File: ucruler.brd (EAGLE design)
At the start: 200 x 32 mm, 46 parts

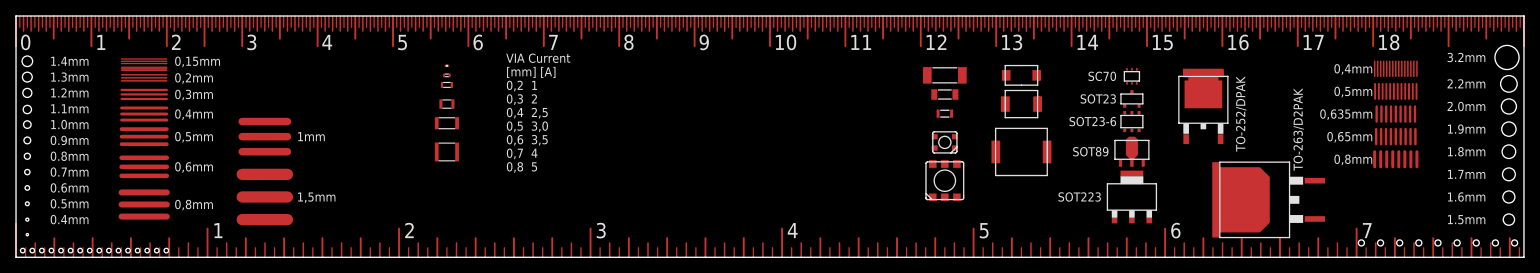
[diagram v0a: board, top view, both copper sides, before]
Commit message: labeled all packages
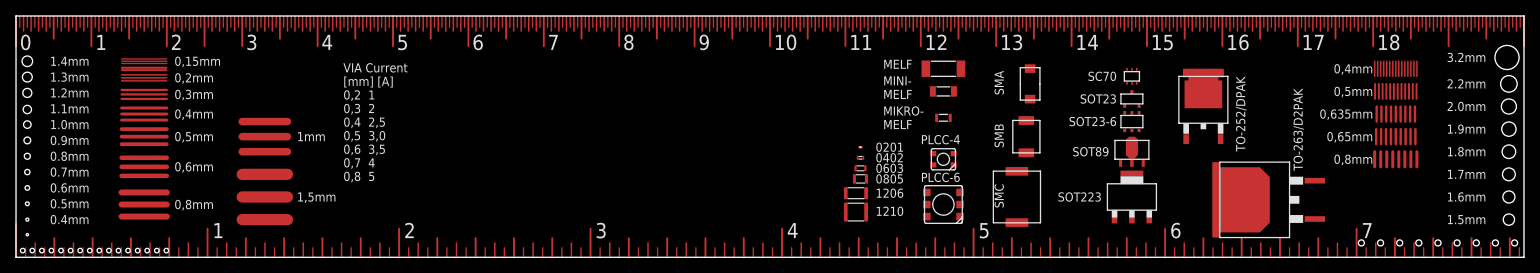
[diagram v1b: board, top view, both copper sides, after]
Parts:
- moved E$43 56.0 mm to (112.0, 11.8), turned to 180 degrees
- moved E$42 55.9 mm to (112.0, 13.2), turned to 180 degrees
- moved E$41 55.9 mm to (112.0, 14.6), turned to 180 degrees
- moved E$44 55.7 mm to (112.0, 10.4), turned to 180 degrees
- moved E$45 55.0 mm to (111.4, 8.50)
- moved E$46 54.8 mm to (111.4, 6.00)
- moved E$34 6.00 mm to (132.8, 8.00), turned to 180 degrees
- moved E$33 4.37 mm to (134.0, 16.0), turned to 180 degrees
- moved E$40 3.17 mm to (123.0, 7.00), turned to 90 degrees
- moved E$39 2.25 mm to (123.0, 13.0)
- moved E$35 1.61 mm to (134.5, 23.0), turned to 180 degrees
- moved E$36 0.89 mm to (123.0, 25.0)
- moved E$38 0.58 mm to (123.0, 18.5), turned to 270 degrees
- moved E$37 0.45 mm to (123.0, 22.0), turned to 270 degrees
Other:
- board text added: "0201"
- board text added: "0402"
- board text added: "0603"
- board text added: "0805"
- board text added: "1206"
- board text added: "1210"
- board text added: "MELF"
- board text added: "MIKRO- MELF"
- board text added: "MINI- MELF"
- board text added: "PLCC-4"
- board text added: "PLCC-6"
- board text added: "SMA"
- board text added: "SMB"
- board text added: "SMC"
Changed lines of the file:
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@@
 <setting verticaltext="up"/>
 </settings>
-<grid distance="0.05" unitdist="inch" unit="mm" style="lines" multiple="1" display="yes" altdistance="0.025" altunitdist="inch" altunit="mm"/>
+<grid distance="1" unitdist="mm" unit="mm" style="lines" multiple="1" display="yes" altdistance="0.25" altunitdist="mm" altunit="mm"/>
 <layers>
 <layer number="1" name="Top" color="4" fill="1" visible="yes" active="yes"/>
@@
 <layer number="14" name="Route14" color="1" fill="6" visible="no" active="no"/>
 <layer number="15" name="Route15" color="4" fill="6" visible="no" active="no"/>
-<layer number="16" name="Bottom" color="1" fill="1" visible="no" active="yes"/>
+<layer number="16" name="Bottom" color="1" fill="1" visible="yes" active="yes"/>
 <layer number="17" name="Pads" color="2" fill="1" visible="yes" active="yes"/>
 <layer number="18" name="Vias" color="2" fill="1" visible="yes" active="yes"/>
@@
 <hole x="193.675" y="1.905" drill="0.8"/>
 <hole x="191.135" y="1.905" drill="0.8"/>
-<text x="65" y="27" size="1.2" layer="21" align="top-left">VIA Current
+<text x="43.41" y="25.73" size="1.2" layer="21" align="top-left">VIA Current
 [mm] [A]
 0,2  1
@@
 <text x="162.43" y="14.02" size="1.2" layer="21" font="fixed" rot="R270" align="center-right">TO-252/DPAK</text>
 <text x="170.05" y="11.48" size="1.2" layer="21" font="fixed" rot="R270" align="center-right">TO-263/D2PAK</text>
+<text x="114" y="5.5" size="1.2" layer="21" ratio="10">1210</text>
+<text x="114" y="7.9" size="1.2" layer="21" ratio="10">1206</text>
+<text x="114" y="14" size="1.2" layer="21" ratio="10">0201</text>
+<text x="114" y="12.6" size="1.2" layer="21" ratio="10">0402</text>
+<text x="114" y="11.2" size="1.2" layer="21" ratio="10">0603</text>
+<text x="114" y="9.8" size="1.2" layer="21" ratio="10">0805</text>
+<text x="131" y="21.5" size="1.2" layer="21" ratio="10" rot="R90">SMA</text>
+<text x="131" y="14.5" size="1.2" layer="21" ratio="10" rot="R90">SMB</text>
+<text x="131" y="6.5" size="1.2" layer="21" ratio="10" rot="R90">SMC</text>
+<text x="115" y="25" size="1.2" layer="21" ratio="10">MELF</text>
+<text x="115" y="21" size="1.2" layer="21" ratio="10">MINI-
+MELF</text>
+<text x="115" y="17" size="1.2" layer="21" ratio="10">MIKRO-
+MELF</text>
+<text x="120" y="15" size="1.2" layer="21" ratio="10">PLCC-4</text>
+<text x="120" y="10" size="1.2" layer="21" ratio="10">PLCC-6</text>
 </plain>
 <attributes>
@@
 <element name="E$31" library="ucruler" package="PACK-TO252" value="" x="157.48" y="17.78"/>
 <element name="E$32" library="ucruler" package="PACK-TO263" value="" x="168.91" y="7.62" rot="R90"/>
-<element name="E$33" library="ucruler" package="PACK-DO214AA-SMB" value="" x="133.35" y="20.32" rot="R90"/>
-<element name="E$34" library="ucruler" package="PACK-DO214AB-SMC" value="" x="133.35" y="13.97" rot="R90"/>
-<element name="E$35" library="ucruler" package="PACK-DO214AC-SMA" value="" x="133.35" y="24.13" rot="R90"/>
-<element name="E$36" library="ucruler" package="PACK-MELF" value="" x="123.19" y="24.13" rot="R90"/>
-<element name="E$37" library="ucruler" package="PACK-MELF-MINI" value="" x="123.19" y="21.59" rot="R90"/>
-<element name="E$38" library="ucruler" package="PACK-MELF-MICRO" value="" x="123.19" y="19.05" rot="R90"/>
-<element name="E$39" library="ucruler" package="PACK-PLCC-4" value="" x="123.19" y="15.24" rot="R90"/>
-<element name="E$40" library="ucruler" package="PACK-PLCC-6" value="" x="123.19" y="10.16"/>
-<element name="E$41" library="ucruler" package="PACK-0201" value="" x="57.15" y="25.4"/>
-<element name="E$42" library="ucruler" package="PACK-0402" value="" x="57.15" y="24.13"/>
-<element name="E$43" library="ucruler" package="PACK-0603" value="" x="57.15" y="22.86"/>
-<element name="E$44" library="ucruler" package="PACK-0805" value="" x="57.15" y="20.32"/>
-<element name="E$45" library="ucruler" package="PACK-1206" value="" x="57.15" y="17.78"/>
-<element name="E$46" library="ucruler" package="PACK-1210" value="" x="57.15" y="13.97"/>
+<element name="E$33" library="ucruler" package="PACK-DO214AA-SMB" value="" x="134" y="16" rot="R180"/>
+<element name="E$34" library="ucruler" package="PACK-DO214AB-SMC" value="" x="132.75" y="8" rot="R180"/>
+<element name="E$35" library="ucruler" package="PACK-DO214AC-SMA" value="" x="134.5" y="23" rot="R180"/>
+<element name="E$36" library="ucruler" package="PACK-MELF" value="" x="123" y="25" rot="R90"/>
+<element name="E$37" library="ucruler" package="PACK-MELF-MINI" value="" x="123" y="22" rot="R270"/>
+<element name="E$38" library="ucruler" package="PACK-MELF-MICRO" value="" x="123" y="18.5" rot="R270"/>
+<element name="E$39" library="ucruler" package="PACK-PLCC-4" value="" x="123" y="13" rot="R90"/>
+<element name="E$40" library="ucruler" package="PACK-PLCC-6" value="" x="123" y="7" rot="R90"/>
+<element name="E$41" library="ucruler" package="PACK-0201" value="" x="112" y="14.6" rot="R180"/>
+<element name="E$42" library="ucruler" package="PACK-0402" value="" x="112" y="13.2" rot="R180"/>
+<element name="E$43" library="ucruler" package="PACK-0603" value="" x="112" y="11.8" rot="R180"/>
+<element name="E$44" library="ucruler" package="PACK-0805" value="" x="112" y="10.4" rot="R180"/>
+<element name="E$45" library="ucruler" package="PACK-1206" value="" x="111.4" y="8.5"/>
+<element name="E$46" library="ucruler" package="PACK-1210" value="" x="111.4" y="6"/>
 </elements>
 <signals>

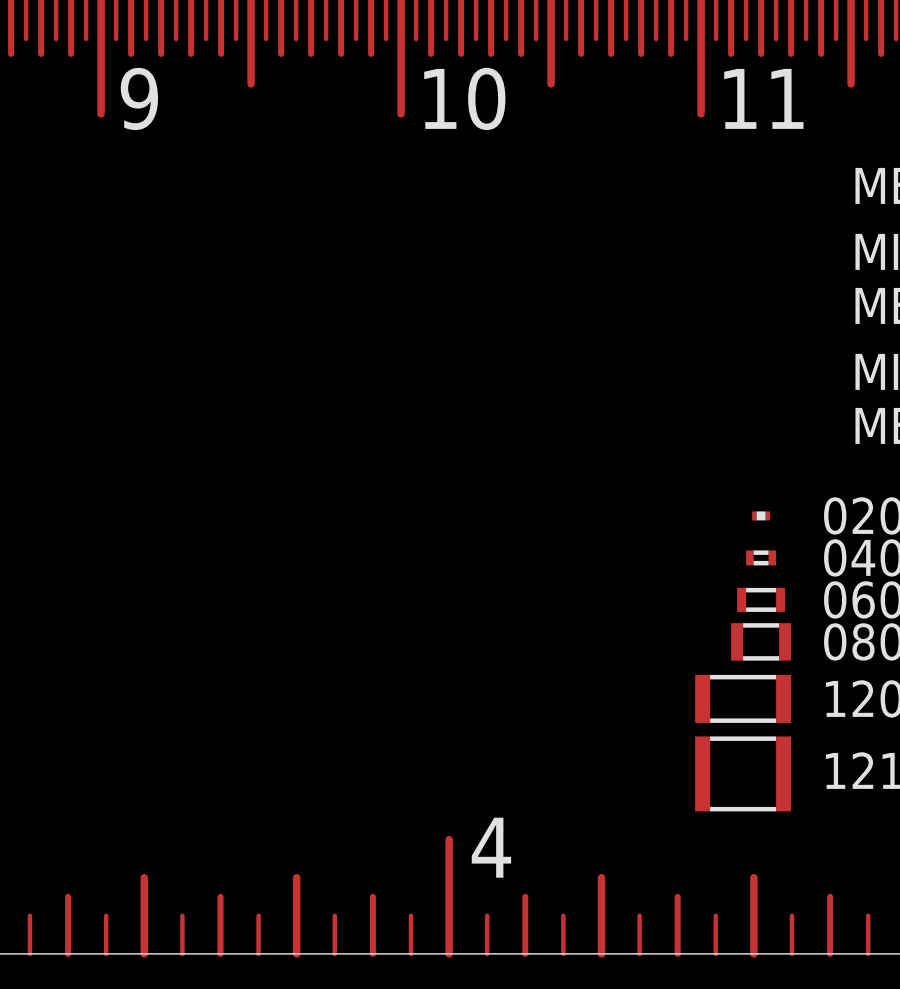
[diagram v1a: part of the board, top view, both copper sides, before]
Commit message: soic n/w 8 to 28 pins
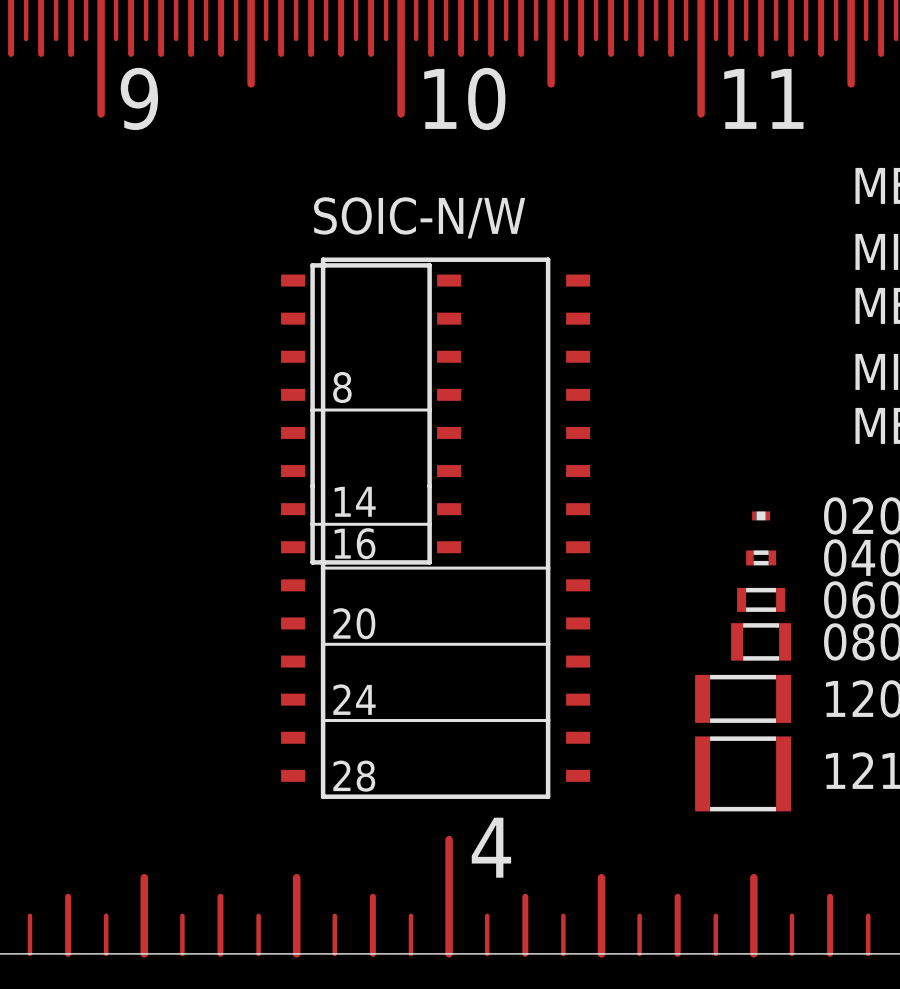
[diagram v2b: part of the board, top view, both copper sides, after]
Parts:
- added E$47: (no value), ucruler:PACK-SOIC
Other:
- board text added: "SOIC-N/W"
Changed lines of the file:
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@@
 <text x="120" y="15" size="1.2" layer="21" ratio="10">PLCC-4</text>
 <text x="120" y="10" size="1.2" layer="21" ratio="10">PLCC-6</text>
+<text x="97" y="24" size="1.2" layer="21" ratio="10">SOIC-N/W</text>
 </plain>
 <attributes>
@@
 <element name="E$45" library="ucruler" package="PACK-1206" value="" x="111.4" y="8.5"/>
 <element name="E$46" library="ucruler" package="PACK-1210" value="" x="111.4" y="6"/>
+<element name="E$47" library="ucruler" package="PACK-SOIC" value="" x="96" y="18"/>
 </elements>
 <signals>

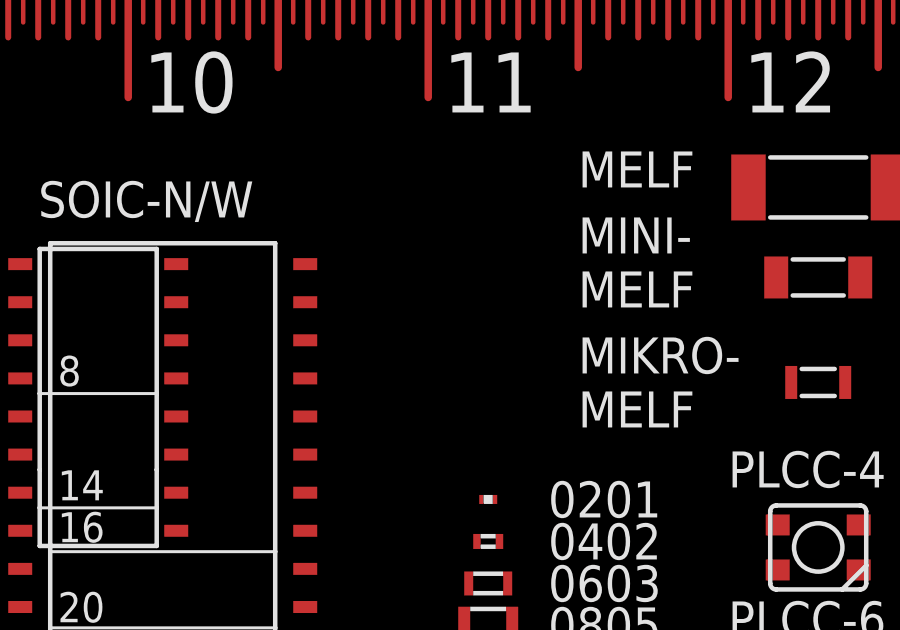
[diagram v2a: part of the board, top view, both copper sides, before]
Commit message: add qfn32
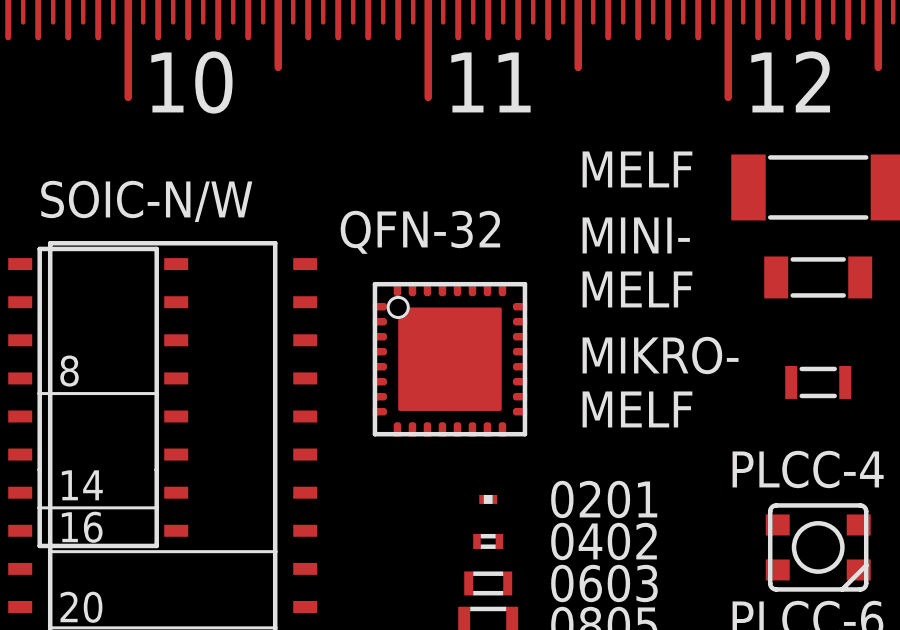
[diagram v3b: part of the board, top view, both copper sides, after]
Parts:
- added E$48: (no value), ucruler:PACK-QFN-32
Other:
- board text added: "QFN-32"
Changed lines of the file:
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@@
 <text x="120" y="10" size="1.2" layer="21" ratio="10">PLCC-6</text>
 <text x="97" y="24" size="1.2" layer="21" ratio="10">SOIC-N/W</text>
+<text x="107" y="23" size="1.2" layer="21" ratio="10">QFN-32</text>
 </plain>
 <attributes>
@@
 <element name="E$46" library="ucruler" package="PACK-1210" value="" x="111.4" y="6"/>
 <element name="E$47" library="ucruler" package="PACK-SOIC" value="" x="96" y="18"/>
+<element name="E$48" library="ucruler" package="PACK-QFN-32" value="" x="109" y="21"/>
 </elements>
 <signals>

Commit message: +sod323/sc76
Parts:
- added E$49: (no value), ucruler:PACK-SOD323
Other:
- board text added: "MINI- MELF/ SOD80"
- board text added: "SOD323/SC76"
- board text removed: "MINI- MELF"
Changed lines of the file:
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@@
 <hole x="180.975" y="1.905" drill="0.8"/>
 <hole x="178.435" y="1.905" drill="0.8"/>
-<text x="146" y="24" size="1.2" layer="21" font="fixed" align="center-right">SC70</text>
-<text x="146" y="21" size="1.2" layer="21" font="fixed" align="center-right">SOT23</text>
-<text x="146" y="18" size="1.2" layer="21" font="fixed" align="center-right">SOT23-6</text>
-<text x="145" y="14" size="1.2" layer="21" font="fixed" align="center-right">SOT89</text>
-<text x="144" y="8" size="1.2" layer="21" font="fixed" align="center-right">SOT223</text>
+<text x="146" y="24" size="1.2" layer="21" font="fixed" distance="20" align="center-right">SC70</text>
+<text x="146" y="21" size="1.2" layer="21" font="fixed" distance="20" align="center-right">SOT23</text>
+<text x="146" y="18" size="1.2" layer="21" font="fixed" distance="20" align="center-right">SOT23-6</text>
+<text x="145" y="14" size="1.2" layer="21" font="fixed" distance="20" align="center-right">SOT89</text>
+<text x="144" y="8" size="1.2" layer="21" font="fixed" distance="20" align="center-right">SOT223</text>
 <rectangle x1="142" y1="3" x2="193" y2="9" layer="22"/>
 <rectangle x1="0" y1="0" x2="3" y2="32" layer="29"/>
@@
 <text x="161.5" y="27" size="0.8" layer="22" ratio="10" rot="MR0">DD</text>
 <text x="161.5" y="10.3" size="0.8" layer="22" ratio="10" rot="MR0">SS</text>
-<text x="162.43" y="14.02" size="1.2" layer="21" font="fixed" rot="R270" align="center-right">TO-252/DPAK</text>
-<text x="170.05" y="11.48" size="1.2" layer="21" font="fixed" rot="R270" align="center-right">TO-263/D2PAK</text>
-<text x="114" y="5.5" size="1.2" layer="21" ratio="10">1210</text>
-<text x="114" y="7.9" size="1.2" layer="21" ratio="10">1206</text>
-<text x="114" y="14" size="1.2" layer="21" ratio="10">0201</text>
-<text x="114" y="12.6" size="1.2" layer="21" ratio="10">0402</text>
-<text x="114" y="11.2" size="1.2" layer="21" ratio="10">0603</text>
-<text x="114" y="9.8" size="1.2" layer="21" ratio="10">0805</text>
-<text x="131" y="21.5" size="1.2" layer="21" ratio="10" rot="R90">SMA</text>
-<text x="131" y="14.5" size="1.2" layer="21" ratio="10" rot="R90">SMB</text>
-<text x="131" y="6.5" size="1.2" layer="21" ratio="10" rot="R90">SMC</text>
-<text x="115" y="25" size="1.2" layer="21" ratio="10">MELF</text>
-<text x="115" y="21" size="1.2" layer="21" ratio="10">MINI-
+<text x="162.43" y="14.02" size="1.2" layer="21" font="fixed" distance="20" rot="R270" align="center-right">TO-252/DPAK</text>
+<text x="170.05" y="11.48" size="1.2" layer="21" font="fixed" distance="20" rot="R270" align="center-right">TO-263/D2PAK</text>
+<text x="114" y="5.5" size="1.2" layer="21" ratio="10" distance="20">1210</text>
+<text x="114" y="7.9" size="1.2" layer="21" ratio="10" distance="20">1206</text>
+<text x="114" y="14" size="1.2" layer="21" ratio="10" distance="20">0201</text>
+<text x="114" y="12.6" size="1.2" layer="21" ratio="10" distance="20">0402</text>
+<text x="114" y="11.2" size="1.2" layer="21" ratio="10" distance="20">0603</text>
+<text x="114" y="9.8" size="1.2" layer="21" ratio="10" distance="20">0805</text>
+<text x="131" y="21.5" size="1.2" layer="21" ratio="10" distance="20" rot="R90">SMA</text>
+<text x="131" y="14.5" size="1.2" layer="21" ratio="10" distance="20" rot="R90">SMB</text>
+<text x="131" y="6.5" size="1.2" layer="21" ratio="10" distance="20" rot="R90">SMC</text>
+<text x="115" y="25" size="1.2" layer="21" ratio="10" distance="20">MELF</text>
+<text x="115" y="20.5" size="1.2" layer="21" ratio="10" distance="20">MINI-
+MELF/
+SOD80</text>
+<text x="115" y="17" size="1.2" layer="21" ratio="10" distance="20">MIKRO-
 MELF</text>
-<text x="115" y="17" size="1.2" layer="21" ratio="10">MIKRO-
-MELF</text>
-<text x="120" y="15" size="1.2" layer="21" ratio="10">PLCC-4</text>
-<text x="120" y="10" size="1.2" layer="21" ratio="10">PLCC-6</text>
-<text x="97" y="24" size="1.2" layer="21" ratio="10">SOIC-N/W</text>
-<text x="107" y="23" size="1.2" layer="21" ratio="10">QFN-32</text>
+<text x="120" y="15" size="1.2" layer="21" ratio="10" distance="20">PLCC-4</text>
+<text x="120" y="10" size="1.2" layer="21" ratio="10" distance="20">PLCC-6</text>
+<text x="97" y="24" size="1.2" layer="21" ratio="10" distance="20">SOIC-N/W</text>
+<text x="107" y="23" size="1.2" layer="21" ratio="10" distance="20">QFN-32</text>
+<text x="128.5" y="14.75" size="1.2" layer="21" ratio="10" distance="20" rot="R90">SOD323/SC76</text>
 </plain>
 <attributes>
@@
 <element name="E$47" library="ucruler" package="PACK-SOIC" value="" x="96" y="18"/>
 <element name="E$48" library="ucruler" package="PACK-QFN-32" value="" x="109" y="21"/>
+<element name="E$49" library="ucruler" package="PACK-SOD323" value="" x="128" y="13"/>
 </elements>
 <signals>
